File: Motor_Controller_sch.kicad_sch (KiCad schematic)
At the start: 40 parts, among them J1 1988804, J10 1988862, J11 Barrel_Jack_Switch, J13 1988862, J14 1988817, J2 GND, J3 RX, J4 TX, J5 RESET, J9 1988862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

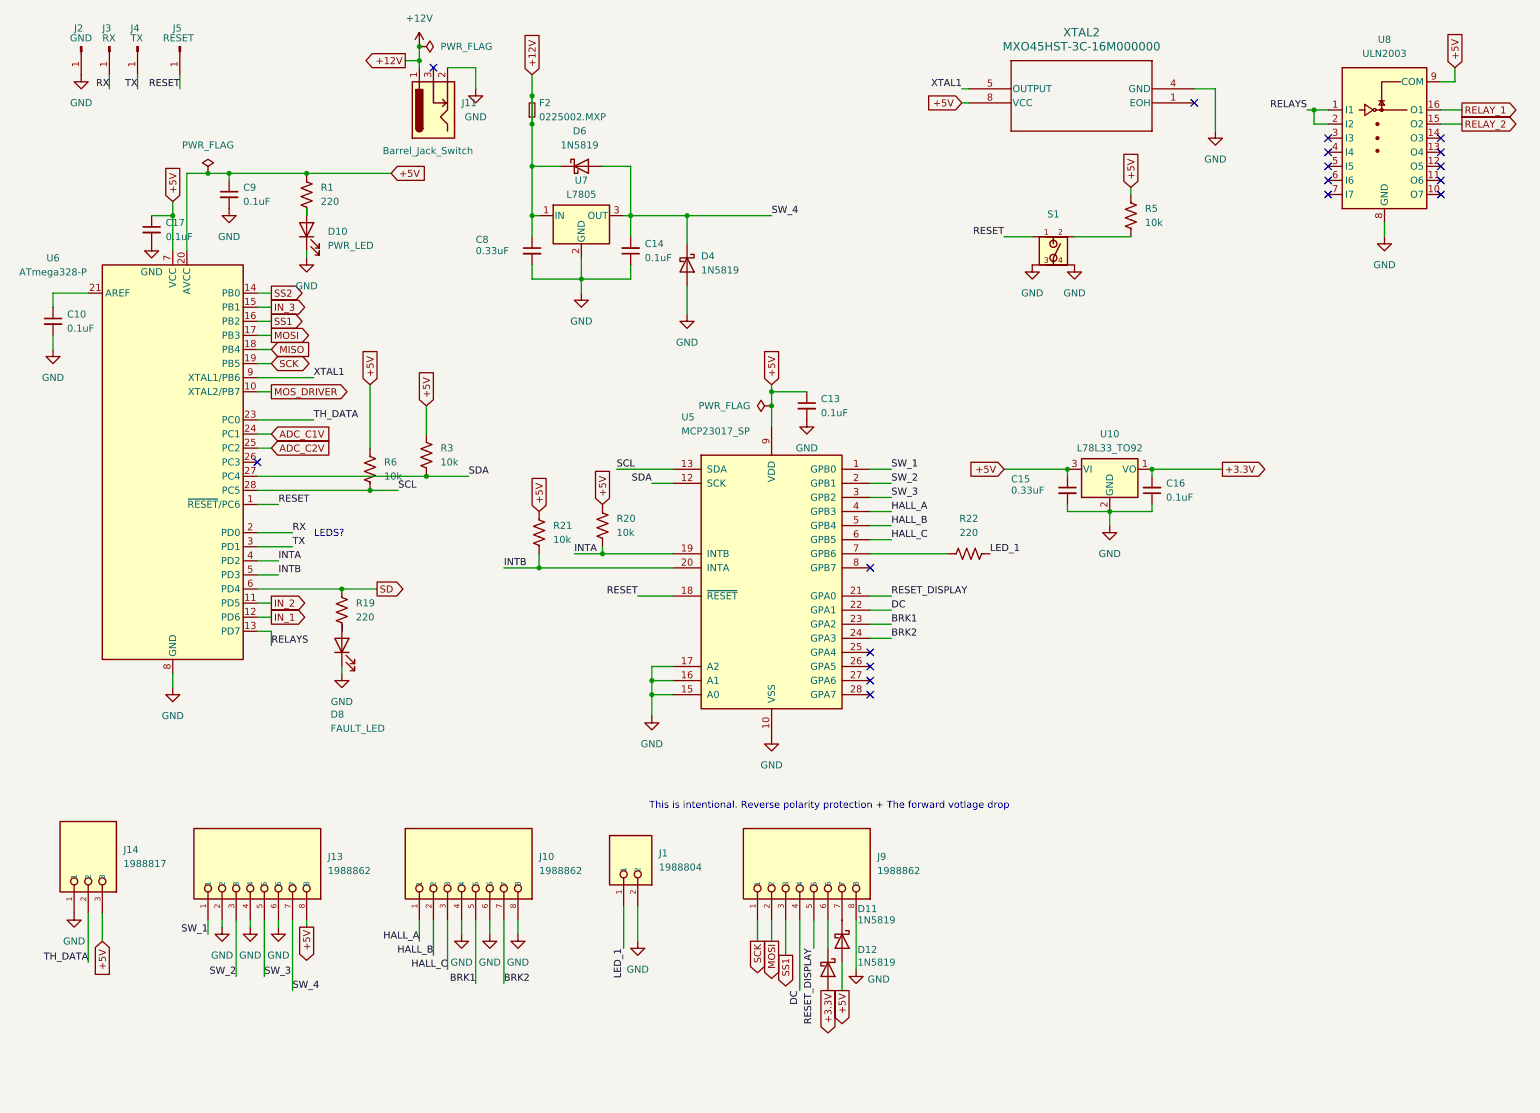
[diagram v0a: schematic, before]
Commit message: Removed a couple redundent VIA's, added +5Vpin
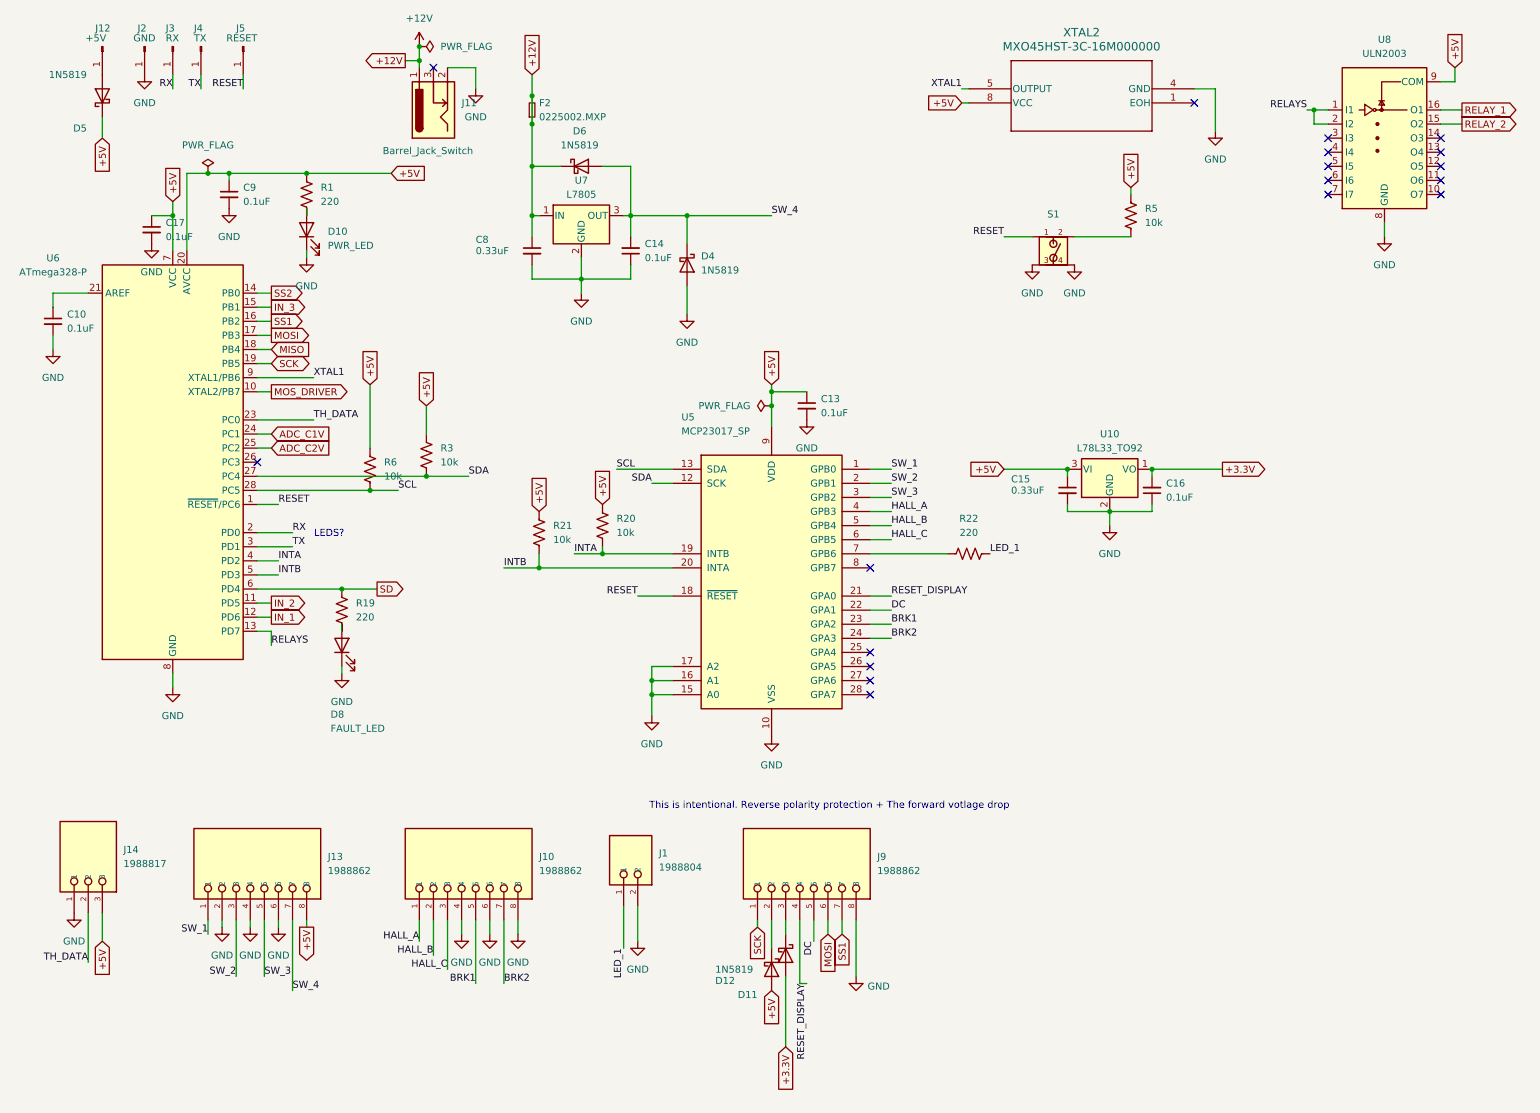
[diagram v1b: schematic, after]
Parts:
- added D5: 1N5819, Diode_THT:D_DO-41_SOD81_P10.16mm_Horizontal, symbol Diode:1N5819
- added J12: +5V, Connector_PinHeader_1.00mm:PinHeader_1x01_P1.00mm_Vertical, symbol Connector:Conn_01x01_Pin
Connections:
- net +3.3V: now also D11.2 (A); no longer D12.2 (A)
- net +5V: now also D12.2 (A), D5.1 (K); no longer D11.2 (A)
- net DC: now also J9.5; no longer J9.4
- net MOSI: now also J9.6; no longer J9.2
- net RESET_DISPLAY: now also J9.4; no longer J9.5
- net SS1: now also J9.7; no longer J9.3
- net at D11.1 (K): now also J9.3; no longer J9.7
- net at D12.1 (K): now also J9.2; no longer J9.6
- new net: D5.2 (A), J12.1 (Pin_1)
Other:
- moved on the sheet: J2, J3, J4, J5

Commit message: Fixed minor inconsistencies, improved orginization, MOSFET gate resistors calculted.
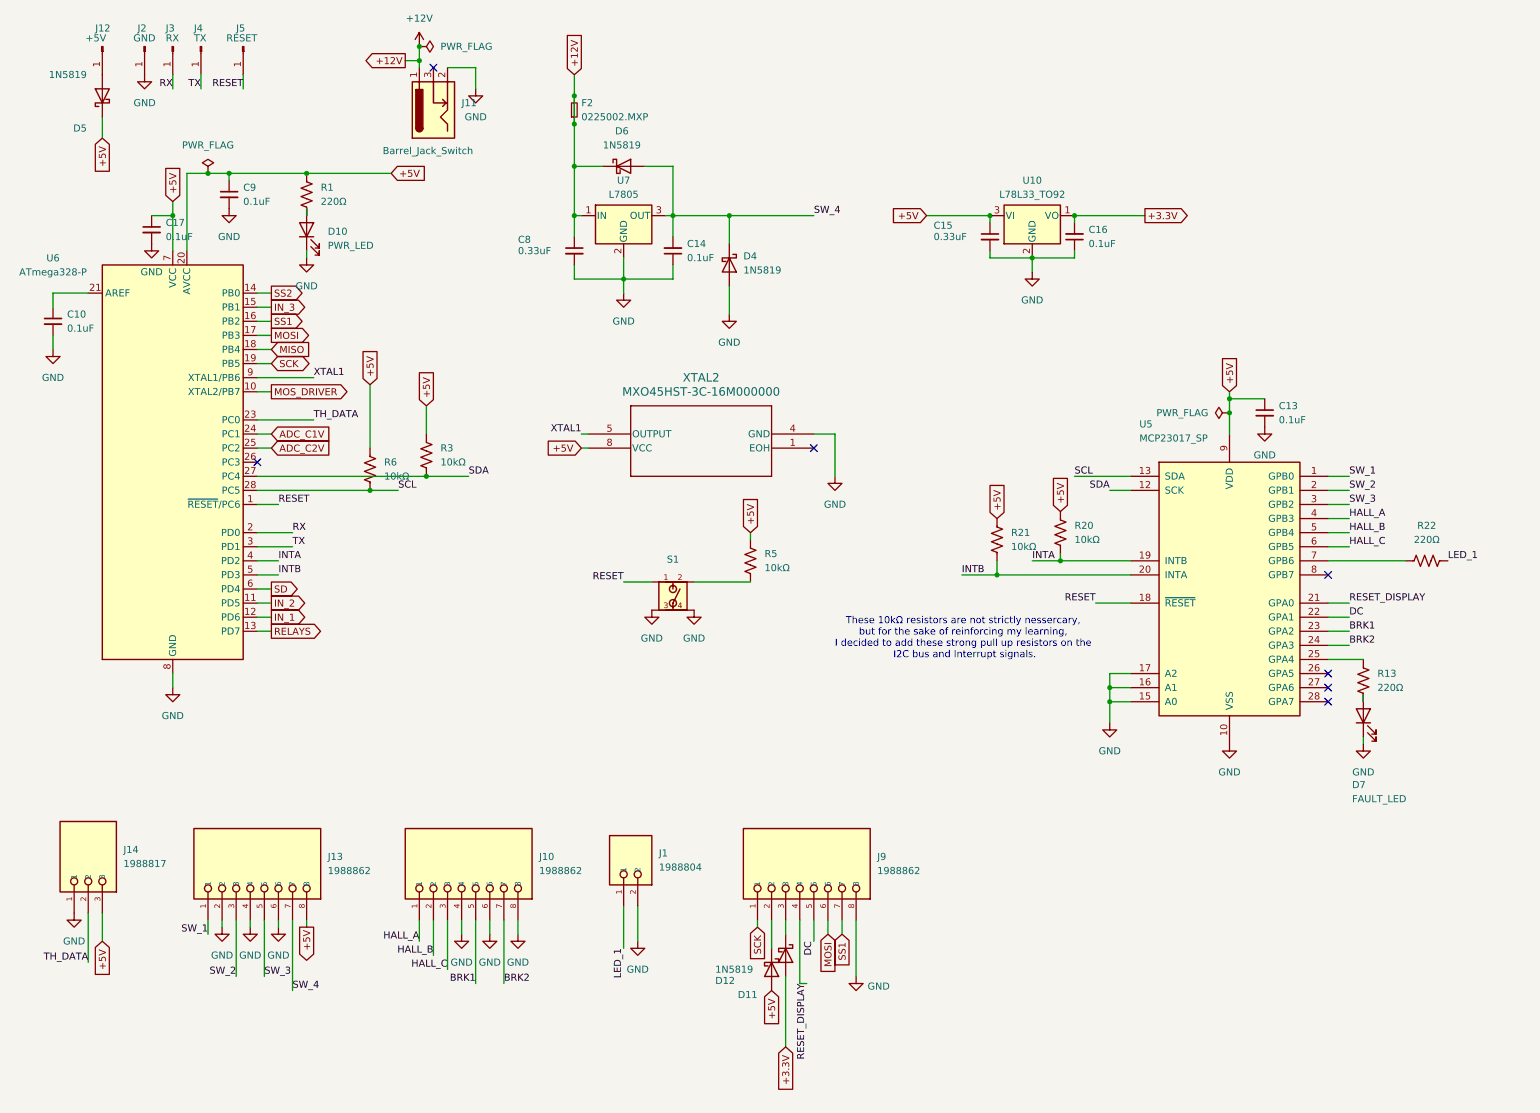
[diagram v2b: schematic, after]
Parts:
- removed D8: FAULT_LED, LED_THT:LED_D5.0mm, symbol Device:LED
- removed R19: 220, Resistor_THT:R_Axial_DIN0207_L6.3mm_D2.5mm_P10.16mm_Horizontal, symbol Device:R_US
- removed U8: ULN2003, Package_DIP:DIP-16_W7.62mm_Socket, symbol Transistor_Array:ULN2003
- added D7: FAULT_LED, LED_THT:LED_D5.0mm, symbol Device:LED
- added R13: 220Ω, Resistor_THT:R_Axial_DIN0207_L6.3mm_D2.5mm_P10.16mm_Horizontal, symbol Device:R_US
- R1, R22: value 220 -> 220Ω
- R20, R21, R3, R5, R6: value 10k -> 10kΩ
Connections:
- net GND: now also D7.1 (K)
- net at U5.25 (GPA4): now also R13.1
- new net: D7.2 (A), R13.2
- no-connect marks 18 -> 7
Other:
- note added: "These 10kΩ resistors are not strictly nessercary, but for the sake of reinforcing my learning, I decided to add these strong pull up resistors on the I2C bus and Interrupt signals."
- note removed: "LEDS?"
- note removed: "This is intentional. Reverse polarity protection + The forward votlage drop"
- moved on the sheet: C13, C14, C15, C16, C8, D4, D6, F2, R20, R21, R22, R5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
